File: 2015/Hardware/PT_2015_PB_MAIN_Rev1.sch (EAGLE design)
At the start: 51 parts, among them Q1 Q_INA28, Q2 Q_INA28, Q4 Q_ACS711LC, Q5 Q_ACS711LC, Q6 Q_IRFS7437PbF

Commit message: Pi-Filter, Regulated outputs, and signals
Added an (unvalued) Pi filter on the output of the 5V critical  bus,
began adding output terminals and LEDs for the regulated outputs, added
an LED to the unregulated output, fixed values, and connected analog
signals to the MCU.
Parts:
- added 12V-AUX: H_20020618-M02, MRDT-2015-PowerBoard:H_20020618-M02
- added C18: 47µF, resistor:C-USC1206
- added L3: (no value), resistor:L-USL3216C
- added LED1, LED2, LED3, LED4, LED5: (no value), SparkFun-LED:LED1206
- added R10, R11, R12, R13, R9: 1kΩ, SparkFun-Passives:RESISTOR1206
- C12, C8: value (none) -> 47µf
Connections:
- net VIN-MEAS renamed PRIMARY-VMEAS
- removed net 5V-CRIT: C17.1, OKI-78SR-5/1.5-W36H.VO
- new net 12V-IMEAS: Q2.OUT, U$1.A2
- new net 5V-IMEAS: Q4.VIOUT, U$1.A1
- new net CRIT-IMEAS: Q5.VIOUT, U$1.A3
- new net M1-IMEAS: Q1.OUT, U$1.A4
- new net N$100: C17.1, L3.1, OKI-78SR-5/1.5-W36H.VO
- new net N$33: U$1.PD5
- new net N$37: U$1.D13~
- new net N$38: U$1.PE2
- new net N$45: R10.1
- new net N$46: LED2.A, R10.2
- new net N$48: LED3.A, R11.2
- new net N$49: R12.1
- new net N$50: LED4.A, R12.2
- new net N$51: R13.1
- new net N$52: LED5.A, R13.2
- net +5V: now also C18.1, L3.2
- net 12V-AUX: now also 12V-AUX.R
- net 12V-CRIT: now also R11.1
- net GND: now also 12V-AUX.L, C18.2, LED1.C, LED2.C, LED3.C, LED4.C, LED5.C
- net N$17: now also U$1.D7; no longer Q2.OUT
- net N$22: now also U$1.PB0; no longer U$1.A1
- net N$23: now also U$1.D11~; no longer U$1.A2
- net N$24: now also U$1.D3~; no longer U$1.A3
- net N$25: now also U$1.D2; no longer U$1.A4
- net N$34: now also U$1.D5~; no longer Q4.VIOUT
- net N$39: now also LED1.A, R9.2; no longer Q5.VIOUT
- net N$40: now also R1.2; no longer R1.1
- net N$41: now also R9.1
- net V_BATT: now also R1.1; no longer R1.2
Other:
- note added: "I don't know what values to use for this Pi-Filter yet!!!"
- note added: "Regulated outputs"
- moved on the sheet: C17, C5, MOTOR_1, OKI-78SR-5/1.5-W36H, R1

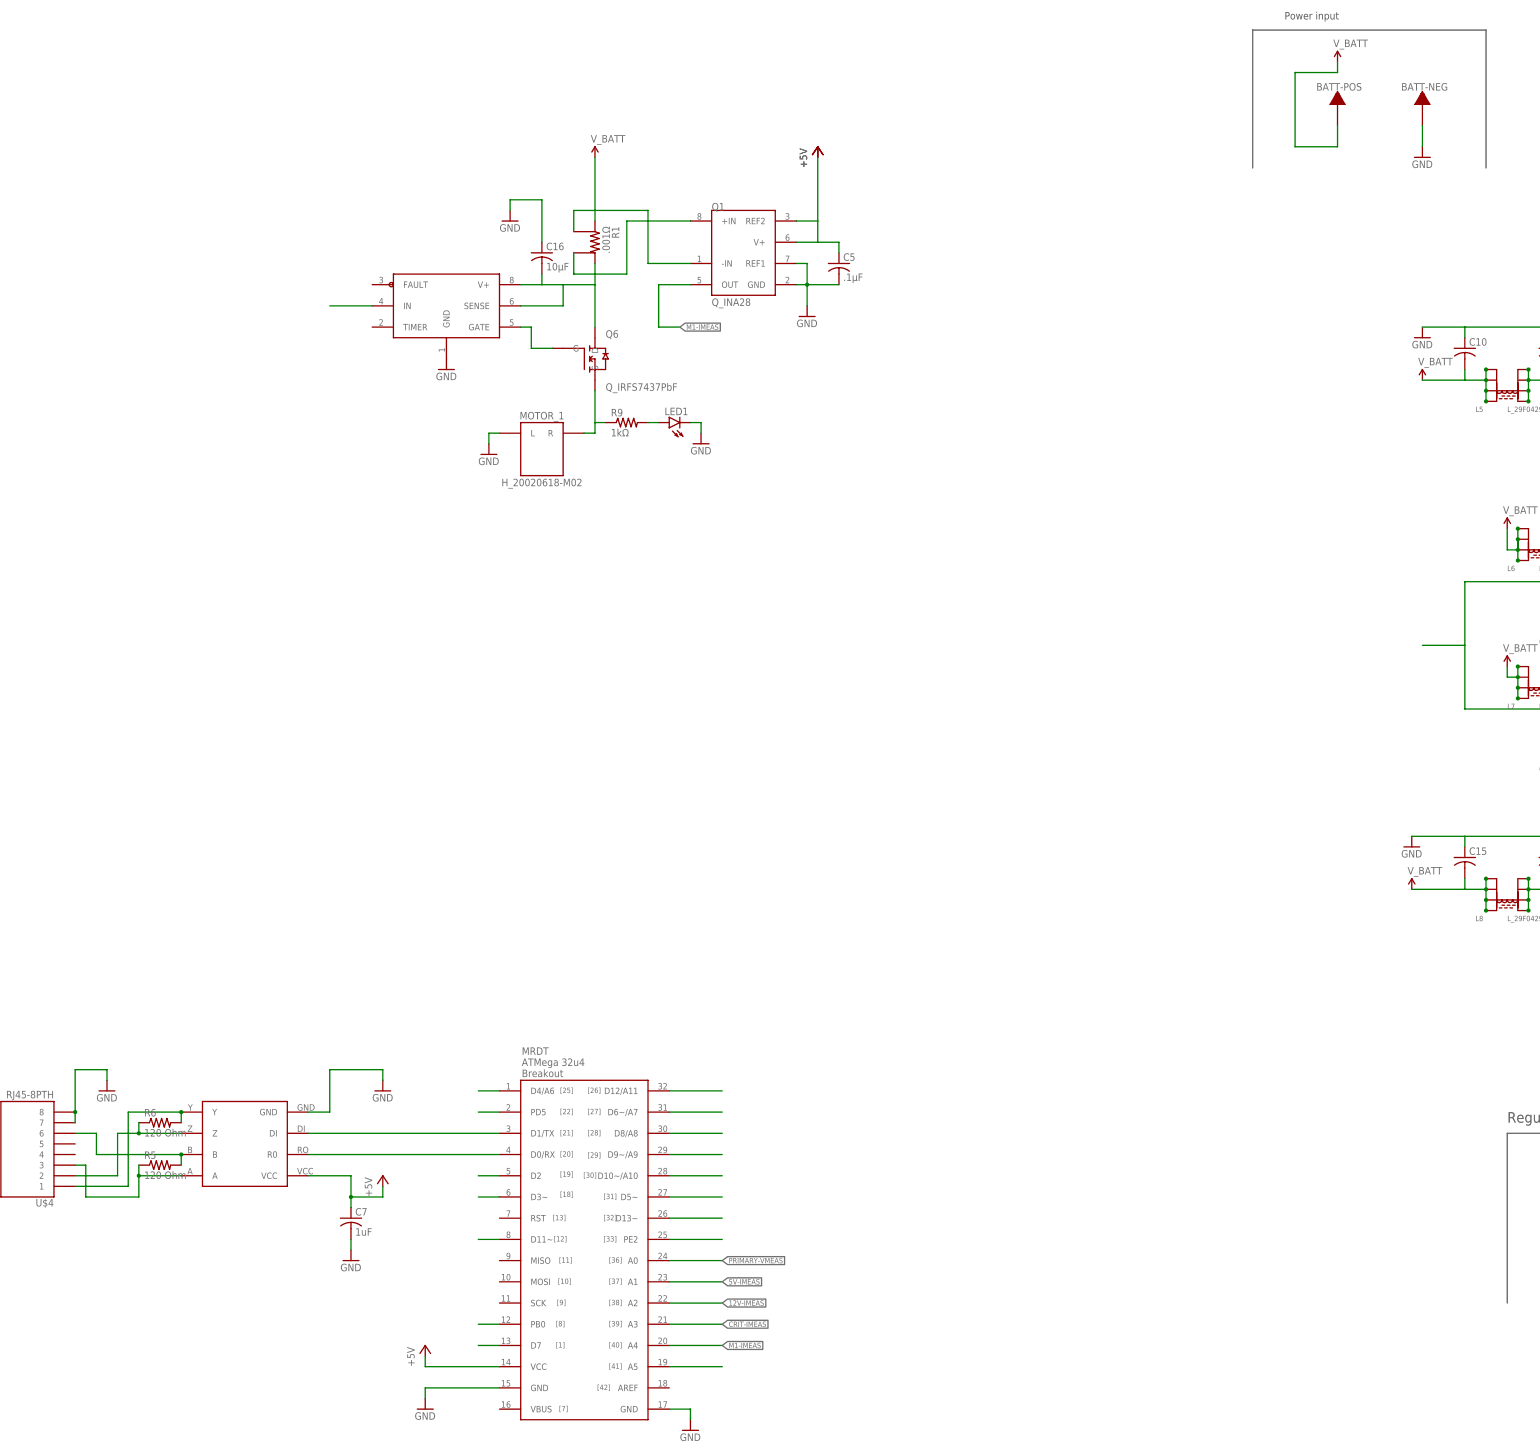
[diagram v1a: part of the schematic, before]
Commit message: Bunch of stuff
Don’t exactly remember. Reading the XML changes, it looks like I
changed a bunch of little things and added a SMD MOSFET to the enable
pin of the 12V Aux bus
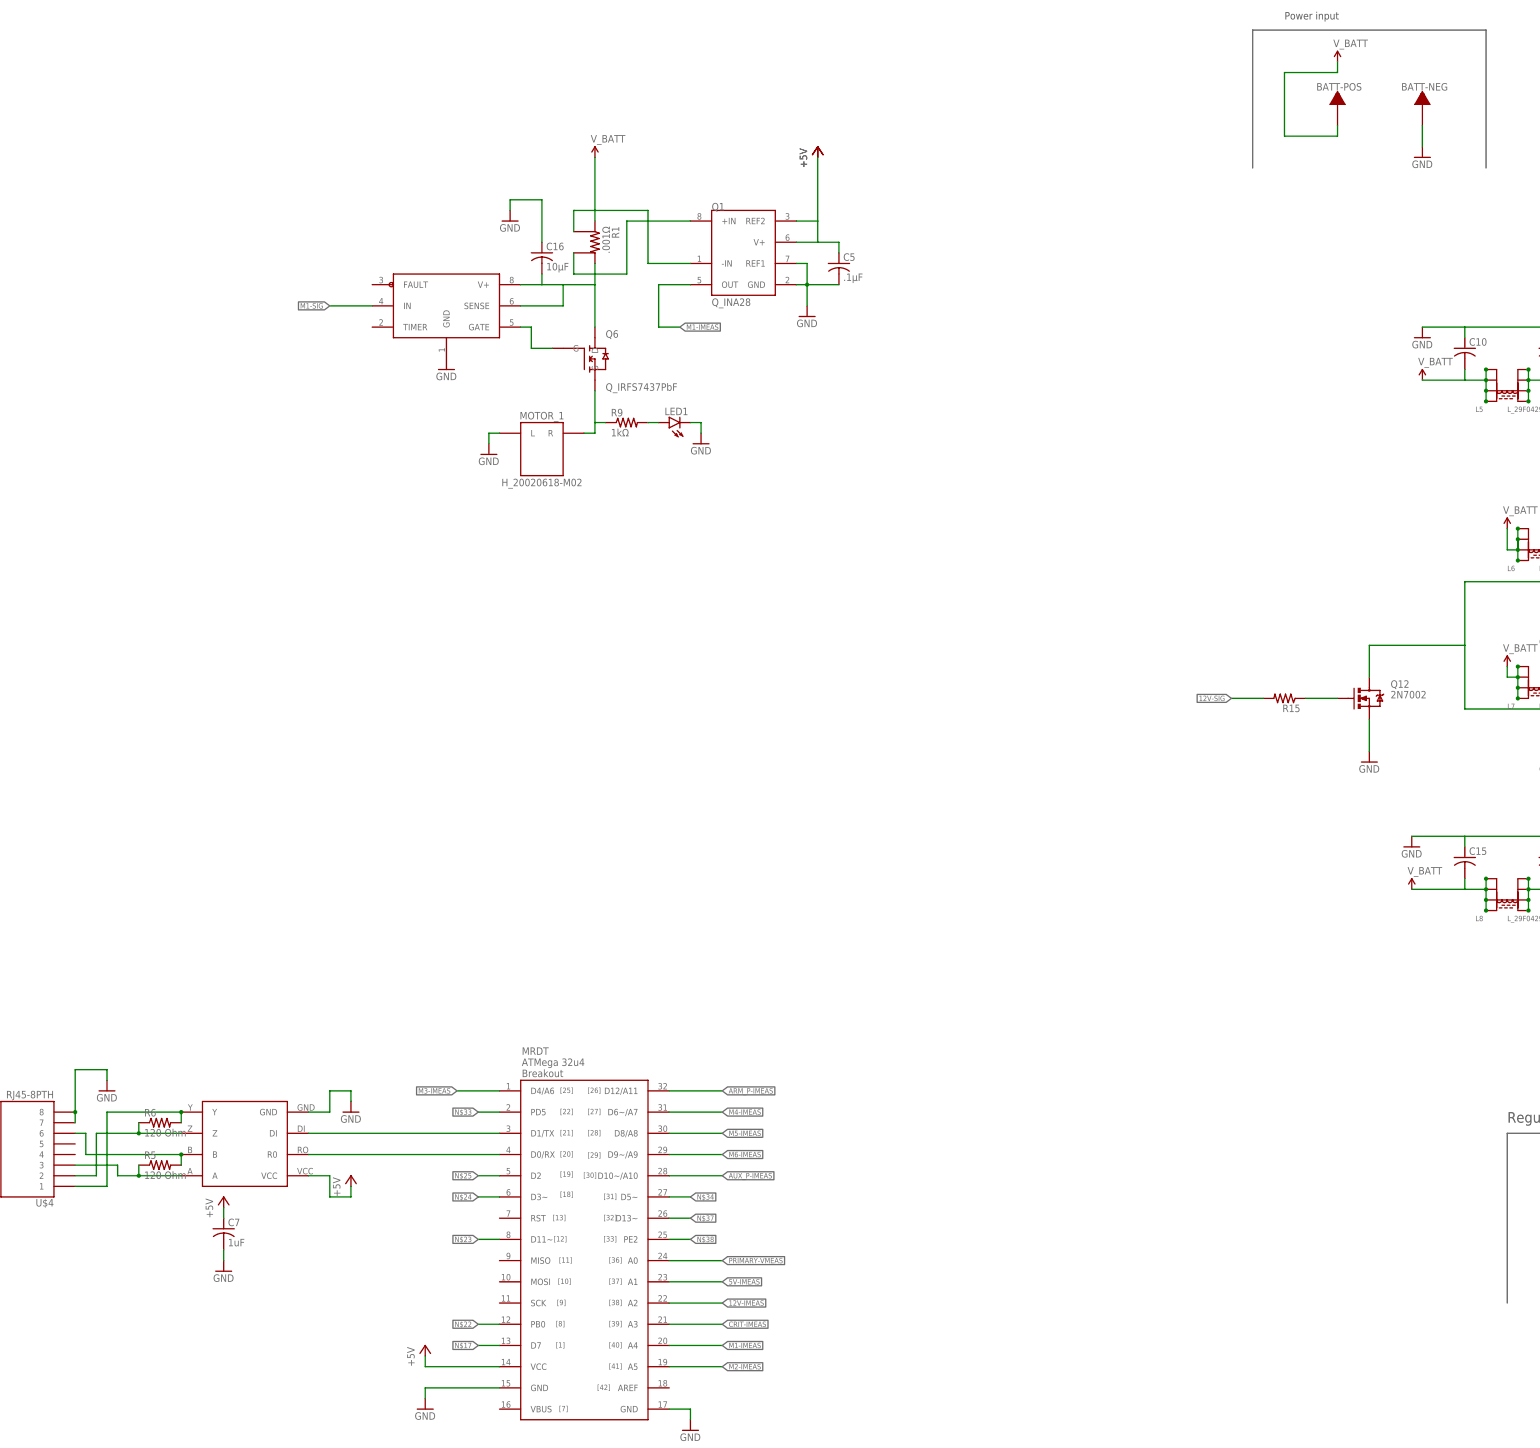
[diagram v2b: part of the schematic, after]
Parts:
- added Q12: 2N7002, SparkFun-DiscreteSemi:MOSFET-NCHANNEL2N7002PW
- added R15: (no value), resistor:R-US_R1206
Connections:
- net N$26 renamed M2-IMEAS
- net N$27 renamed M3-IMEAS
- net N$28 renamed M4-IMEAS
- net N$29 renamed M5-IMEAS
- net N$30 renamed M6-IMEAS
- net N$31 renamed AUX_P-IMEAS
- net N$32 renamed ARM_P-IMEAS
- net N$43 renamed M1-SIG
- new net 12V-SIG: R15.2
- new net N$114: Q12.G, R15.1
- net GND: now also Q12.S
- net N$4: now also Q12.D
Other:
- moved on the sheet: C7

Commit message: Added 7 more Primary Voltage Busses
Copied and pasted a lot. At this point, much of the schematic is good
to go.
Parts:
- added 12V-CRIT, 5V-EXT, 5V-INT: H_WR-TBL_3210002HORIZ, MRDT-2015-PowerBoard:H_WR-TBL_3210002HORIZ
- added ARM_P, AUX_P, MOTOR_2, MOTOR_3, MOTOR_4, MOTOR_5, MOTOR_6: H_20020618-M02, MRDT-2015-PowerBoard:H_20020618-M02
- added C19, C20: (no value), resistor:C-USC1206
- added C21, C22: 330µF, resistor:CPOL-USE5-8.5
- added C23, C25, C27, C29, C31, C33, C35: .1µF, resistor:C-USC1206
- added C24, C26, C28, C30, C32, C34, C36: 10µF, resistor:C-USC1206
- added LED10, LED11, LED12, LED6, LED7, LED8, LED9: (no value), SparkFun-LED:LED1206
- added Q10, Q13, Q15, Q17, Q19, Q3, Q8: Q_INA28, MRDT-2014-All:Q_INA28
- added Q11, Q14, Q16, Q18, Q20, Q7, Q9: Q_IRFS7437PbF, MRDT-2015-PowerBoard:Q_IRF7437SMD
- added R14, R17, R19, R21, R23, R25, R27: .001Ω, MRDT-2014-All:R_FC4L110R001JER
- added R16, R18, R20, R22, R24, R26, R28: 1kΩ, SparkFun-Passives:RESISTOR1206
- added U$10, U$11, U$12, U$13, U$7, U$8, U$9: LT1910, Jake:LT1910
- C13, C14: value (none) -> 2.2µF
- R7: value (none) -> 585Ω
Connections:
- removed net N$17: U$1.D7
- removed net N$22: U$1.PB0
- removed net N$23: U$1.D11~
- removed net N$24: U$1.D3~
- removed net N$25: U$1.D2
- removed net N$33: U$1.PD5
- removed net N$34: U$1.D5~
- removed net N$37: U$1.D13~
- removed net N$38: U$1.PE2
- new net ARM_P-SIG: U$1.D5~, U$12.IN
- new net AUX_P-SIG: U$1.D13~, U$13.IN
- new net M2-SIG: U$1.D2, U$7.IN
- new net M3-SIG: U$1.D3~, U$11.IN
- new net M4-SIG: U$1.D11~, U$8.IN
- new net M5-SIG: U$1.PB0, U$9.IN
- new net M6-SIG: U$1.D7, U$10.IN
- new net N$26: Q3.+IN, R14.SENSE2
- new net N$27: Q3.-IN, R14.SENSE1
- new net N$28: C24.2, Q7.D, R14.2, U$7.SENSE, U$7.V+
- new net N$29: MOTOR_2.R, Q7.S, R16.1
- new net N$30: Q7.G, U$7.GATE
- new net N$31: LED6.A, R16.2
- new net N$32: Q8.+IN, R17.SENSE2
- new net N$43: Q8.-IN, R17.SENSE1
- new net N$44: C26.2, Q9.D, R17.2, U$8.SENSE, U$8.V+
- new net N$47: Q9.G, U$8.GATE
- new net N$53: Q10.-IN, R19.SENSE1
- new net N$54: C28.2, Q11.D, R19.2, U$9.SENSE, U$9.V+
- new net N$55: MOTOR_4.R, Q11.S, R20.1
- new net N$56: Q11.G, U$9.GATE
- new net N$57: LED8.A, R20.2
- new net N$58: Q13.+IN, R21.SENSE2
- new net N$59: Q13.-IN, R21.SENSE1
- new net N$60: C30.2, Q14.D, R21.2, U$10.SENSE, U$10.V+
- new net N$61: MOTOR_5.R, Q14.S, R22.1
- new net N$62: Q14.G, U$10.GATE
- new net N$63: LED9.A, R22.2
- new net N$64: Q15.+IN, R23.SENSE2
- new net N$65: Q15.-IN, R23.SENSE1
- new net N$66: C32.2, Q16.D, R23.2, U$11.SENSE, U$11.V+
- new net N$67: MOTOR_6.R, Q16.S, R24.1
- new net N$68: Q16.G, U$11.GATE
- new net N$69: LED10.A, R24.2
- new net N$70: Q17.+IN, R25.SENSE2
- new net N$71: Q17.-IN, R25.SENSE1
- new net N$72: C34.2, Q18.D, R25.2, U$12.SENSE, U$12.V+
- new net N$73: ARM_P.R, Q18.S, R26.1
- new net N$74: Q18.G, U$12.GATE
- new net N$75: LED11.A, R26.2
- new net N$76: Q19.+IN, R27.SENSE2
- new net N$77: Q19.-IN, R27.SENSE1
- new net N$78: C36.2, Q20.D, R27.2, U$13.SENSE, U$13.V+
- new net N$79: AUX_P.R, Q20.S, R28.1
- new net N$80: Q20.G, U$13.GATE
- new net N$81: LED12.A, R28.2
- net +5V: now also 5V-INT.R, C23.1, C25.1, C27.1, C29.1, C31.1, C33.1, C35.1, Q10.REF2, Q10.V+, Q13.REF2, Q13.V+, Q15.REF2, Q15.V+, Q17.REF2, Q17.V+, Q19.REF2, Q19.V+, Q3.REF2, Q3.V+, Q8.REF2, Q8.V+, R13.1
- net 12V-AUX: now also R10.1
- net 12V-CRIT: now also 12V-CRIT.R
- net 12V-SIG: now also U$1.PE2
- net 5V-EXT: now also 5V-EXT.R, R12.1
- net ARM_P-IMEAS: now also Q17.OUT
- net AUX_P-IMEAS: now also Q19.OUT
- net GND: now also 12V-CRIT.L, 5V-EXT.L, 5V-INT.L, ARM_P.L, AUX_P.L, C19.2, C20.2, C21.-, C22.-, C23.2, C24.1, C25.2, C26.1, C27.2, C28.1, C29.2, C30.1, C31.2, C32.1, C33.2, C34.1, C35.2, C36.1, LED10.C, LED11.C, LED12.C, LED6.C, LED7.C, LED8.C, LED9.C, MOTOR_2.L, MOTOR_3.L, MOTOR_4.L, MOTOR_5.L, MOTOR_6.L, Q10.GND, Q10.REF1, Q13.GND, Q13.REF1, Q15.GND, Q15.REF1, Q17.GND, Q17.REF1, Q19.GND, Q19.REF1, Q3.GND, Q3.REF1, Q8.GND, Q8.REF1, U$10.GND, U$11.GND, U$12.GND, U$13.GND, U$7.GND, U$8.GND, U$9.GND
- net M1-SIG: now also U$1.PD5
- net M2-IMEAS: now also Q3.OUT
- net M3-IMEAS: now also Q15.OUT
- net M4-IMEAS: now also Q8.OUT
- net M5-IMEAS: now also Q10.OUT
- net M6-IMEAS: now also Q13.OUT
- net N$11: now also C20.1
- net N$15: now also C22.+
- net N$36: now also C21.+
- net N$45: now also MOTOR_3.R, Q9.S, R18.1; no longer R10.1
- net N$49: now also LED7.A, R18.2; no longer R12.1
- net N$51: now also Q10.+IN, R19.SENSE2; no longer R13.1
- net N$7: now also C19.1
- net V_BATT: now also R14.1, R17.1, R19.1, R21.1, R23.1, R25.1, R27.1
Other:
- moved on the sheet: C16, C5, LED1, LED3, LED4, LED5, MOTOR_1, Q1, Q6, R1, R11, R12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

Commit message: Erectile Function
;)
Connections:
- net 12V-IMEAS: now also U$1.D12/A11; no longer U$1.A2
- net 12V-SIG: now also U$1.PD5; no longer U$1.PE2
- net 5V-IMEAS: now also U$1.D8/A8; no longer U$1.A1
- net ARM_P-IMEAS: now also U$1.A5; no longer U$1.D12/A11
- net ARM_P-SIG: now also U$1.D7; no longer U$1.D5~
- net AUX_P-IMEAS: now also U$1.A4; no longer U$1.D10~/A10
- net AUX_P-SIG: now also U$1.PB0; no longer U$1.D13~
- net CRIT-IMEAS: now also U$1.D6~/A7; no longer U$1.A3
- net M1-IMEAS: now also U$1.D9~/A9; no longer U$1.A4
- net M1-SIG: now also U$1.D5~; no longer U$1.PD5
- net M2-IMEAS: now also U$1.D10~/A10; no longer U$1.A5
- net M2-SIG: now also U$1.D13~; no longer U$1.D2
- net M3-IMEAS: now also Q8.OUT, U$1.A0; no longer Q15.OUT, U$1.D4/A6
- net M3-SIG: now also U$1.PE2, U$8.IN; no longer U$1.D3~, U$11.IN
- net M4-IMEAS: now also Q10.OUT, U$1.A1; no longer Q8.OUT, U$1.D6~/A7
- net M4-SIG: now also U$1.D2, U$9.IN; no longer U$1.D11~, U$8.IN
- net M5-IMEAS: now also Q13.OUT, U$1.A2; no longer Q10.OUT, U$1.D8/A8
- net M5-SIG: now also U$1.D3~, U$10.IN; no longer U$1.PB0, U$9.IN
- net M6-IMEAS: now also Q15.OUT, U$1.A3; no longer Q13.OUT, U$1.D9~/A9
- net M6-SIG: now also U$1.D11~, U$11.IN; no longer U$1.D7, U$10.IN
- net PRIMARY-VMEAS: now also U$1.D4/A6; no longer U$1.A0
